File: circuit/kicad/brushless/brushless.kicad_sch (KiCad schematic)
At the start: 16 parts, among them J1 MOTOR_OUTPUT, J2 POWER_INPUT, Q1 IRF540N, Q2 IRF540N, Q3 IRF540N

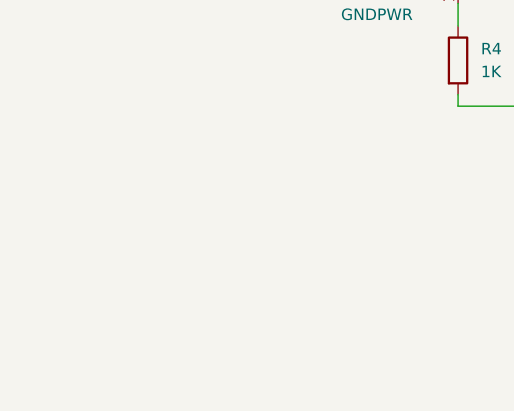
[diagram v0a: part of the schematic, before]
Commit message: UVW BLDC Example
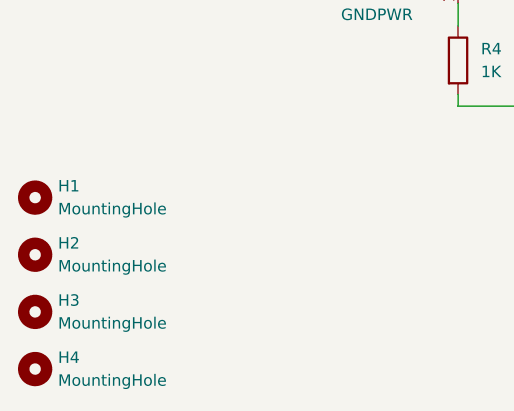
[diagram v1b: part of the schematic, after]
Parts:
- added H1, H2, H3, H4: MountingHole, MountingHole:MountingHole_2.5mm, symbol Mechanical:MountingHole
- D1, D2, D3, D4, D5, D6: footprint (none) -> Diode_SMD:D_SMA-SMB_Universal_Handsoldering
- J1: footprint (none) -> TerminalBlock_Altech:Altech_AK300_1x04_P5.00mm_45-Degree
- J2: footprint (none) -> TerminalBlock_Altech:Altech_AK300_1x02_P5.00mm_45-Degree
- Q1, Q2, Q3: footprint Package_TO_SOT_THT:TO-220-3_Vertical -> Package_TO_SOT_SMD:TO-263-2
- R1, R2, R3, R4: footprint (none) -> Resistor_SMD:R_1206_3216Metric_Pad1.30x1.75mm_HandSolder
- RV1: footprint (none) -> Potentiometer_THT:Potentiometer_Bourns_3266W_Vertical
